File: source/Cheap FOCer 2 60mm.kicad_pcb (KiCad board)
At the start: 2 copper layers, 59.1 x 99.9 mm, 193 parts, among them J1 Conn_01x02, J2 Conn_01x07, J3 Conn_01x03, J4 On/Off, J5 UNUSED MCU PINS, J6 Conn_01x03, P1 MOTOR1, P2 MOTOR1, P3 MOTOR1, P4 HALL/Encoder, P5 SWD, Q1 NCEP60T20, Q2 NCEP60T20, Q3 NCEP60T20, Q4 NCEP60T20, Q5 NCEP60T20, Q6 NCEP60T20, U1 AMS1117-3.3, U2 DRV8301, U3 TP2604-SR, U4 TJA1051T/3/1J, U5 STM32F405RGT6, U6 BMI160, X1 8MHz 10ppm (X50328MSB2GI)

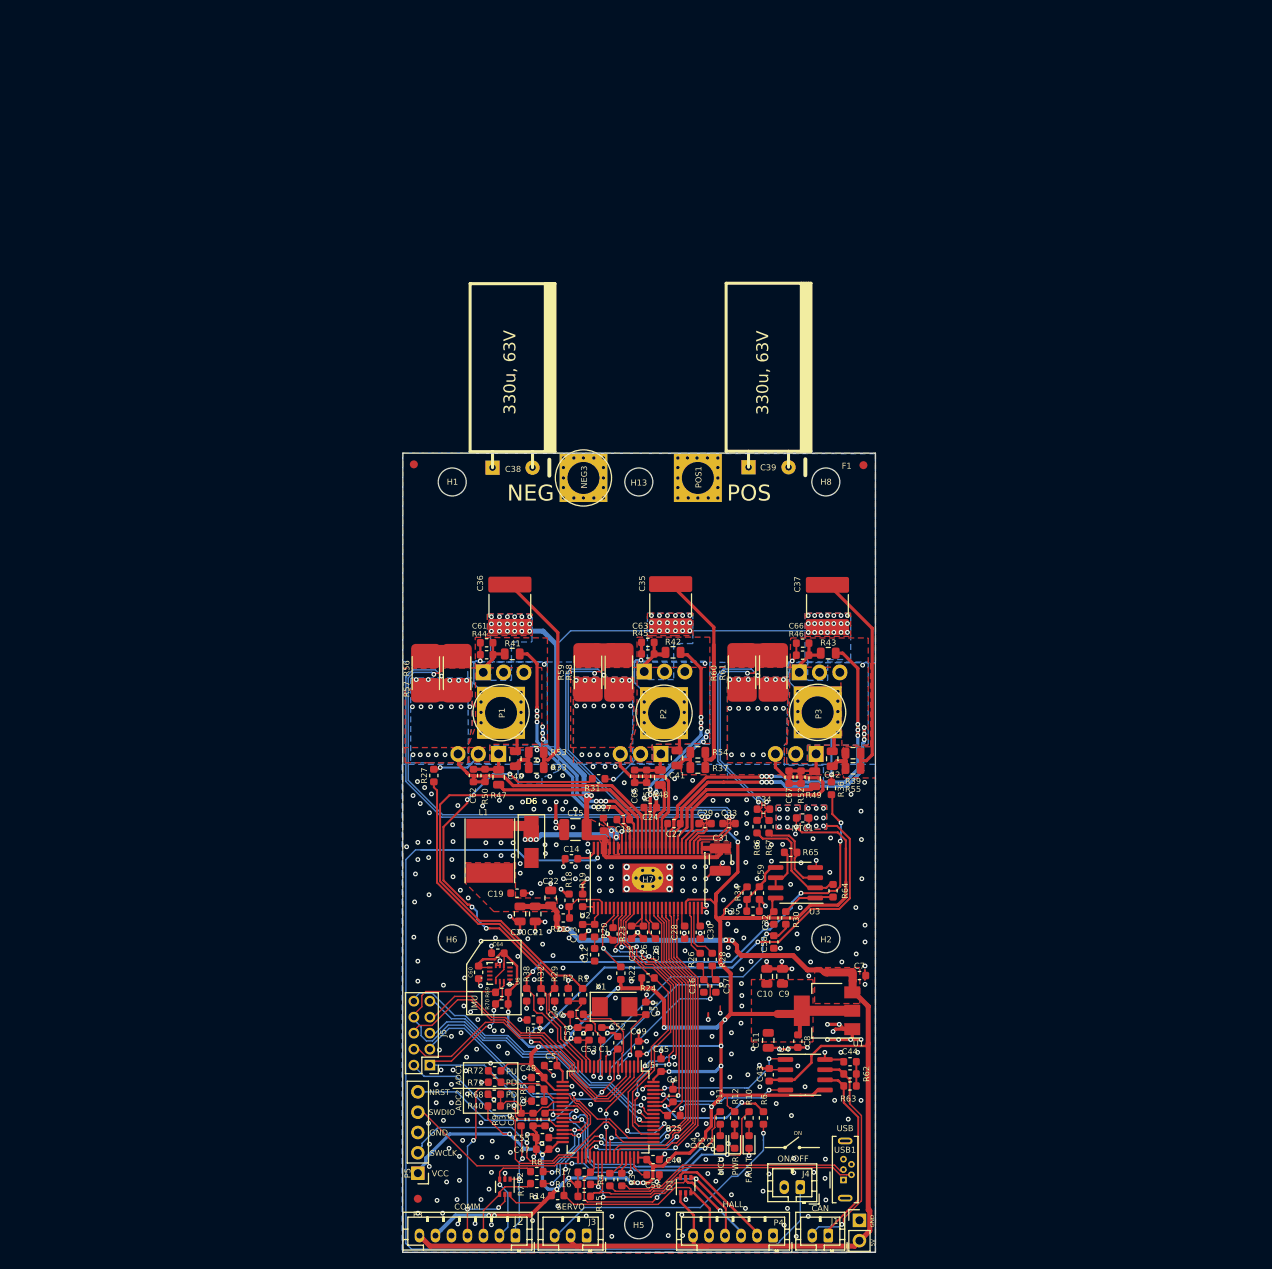
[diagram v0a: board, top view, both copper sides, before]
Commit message: started redrawing pcb
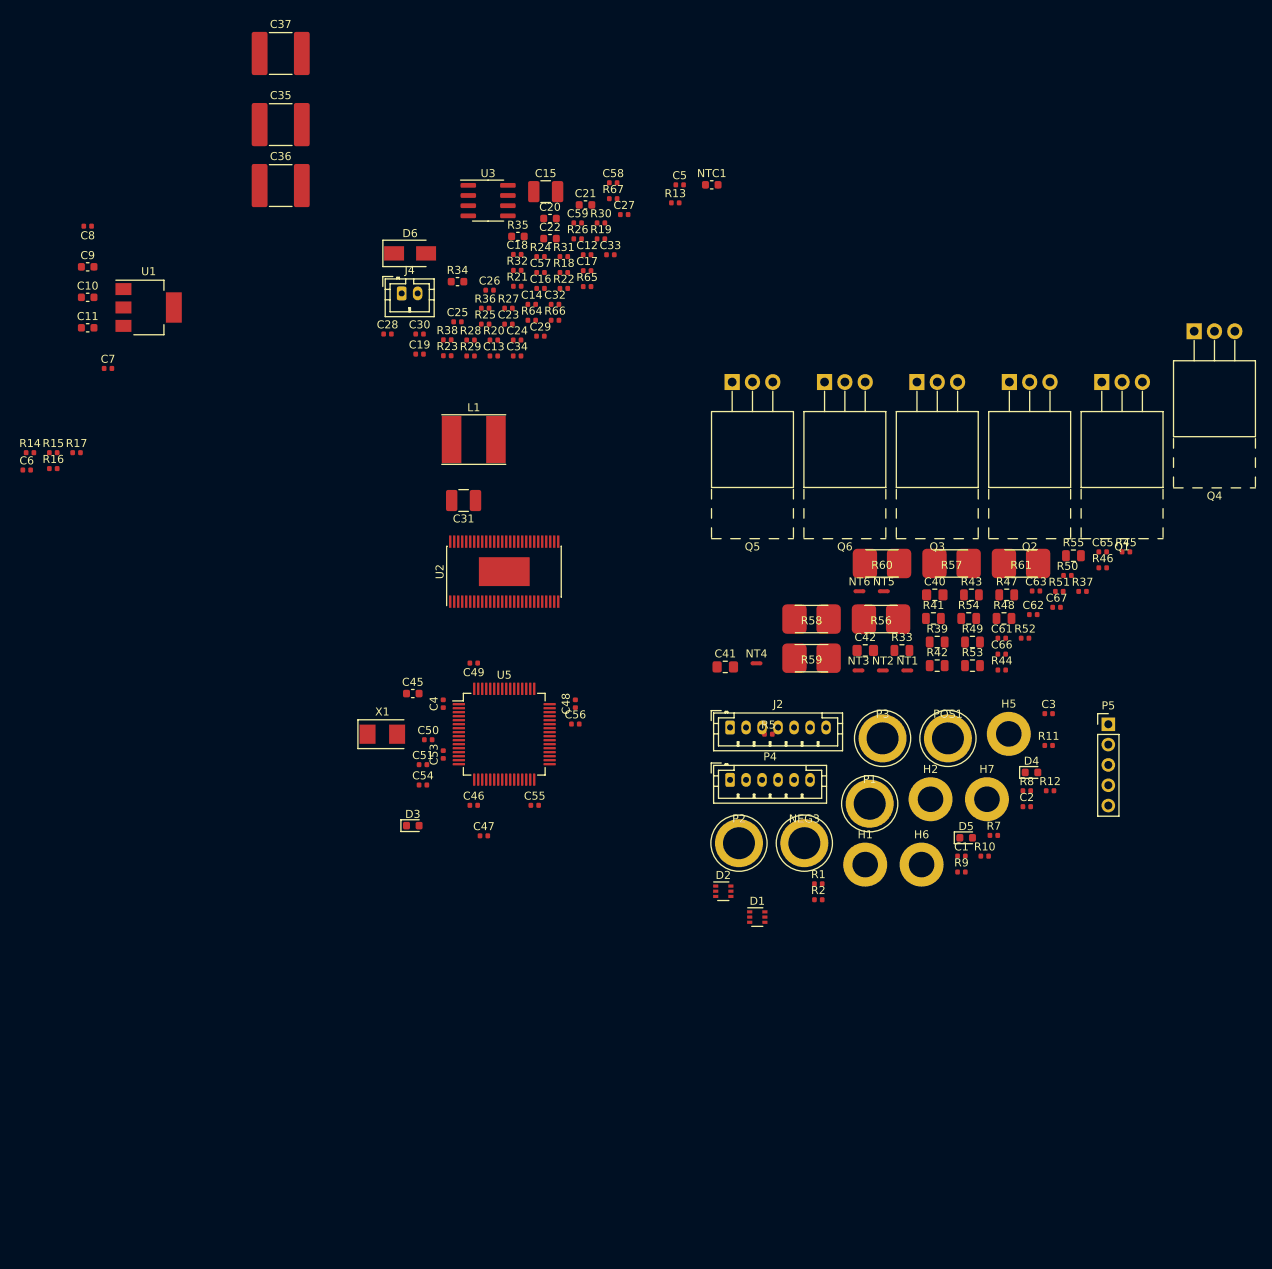
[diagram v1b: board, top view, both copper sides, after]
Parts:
- removed C38, C39: 330u, 63V, w_capacitors:CP_10x20mm_hor_with_model_brd_edge
- removed C43: 0.1u, Capacitor_SMD:C_0603_1608Metric
- removed C44: 1nF, Capacitor_SMD:C_0603_1608Metric
- removed C52, C60, C64: 100n, Capacitor_SMD:C_0603_1608Metric
- removed F1, F2, F3: Fiducial, Fiducial:Fiducial_1mm_Dia_2mm_Outer
- removed H13, H8: MountingHole, MountingHole:MountingHole_3.2mm_M3_ISO14580_Pad
- removed H3: SLJ, shapes3D:Sam_J
- removed H4: Open Hardware Logo, Symbol:OSHW-Logo2_9.8x8mm_SilkScreen
- removed H9: KiCAD Logo, Symbol:KiCad-Logo2_5mm_SilkScreen
- removed J1: Conn_01x02, Connector_JST:JST_PH_B2B-PH-K_1x02_P2.00mm_Vertical
- removed J3: Conn_01x03, Connector_JST:JST_PH_B3B-PH-K_1x03_P2.00mm_Vertical
- removed J5: UNUSED MCU PINS, Connector_PinHeader_2.00mm:PinHeader_2x05_P2.00mm_Vertical
- removed J6: Conn_01x03, Connector_PinHeader_2.54mm:PinHeader_1x02_P2.54mm_Vertical
- removed R3, R4: 22R, Resistor_SMD:R_0603_1608Metric
- removed R40, R68, R71, R72: DNP, Resistor_SMD:R_0603_1608Metric
- removed R6: 100R, Resistor_SMD:R_0603_1608Metric
- removed R62, R63: 60, Resistor_SMD:R_0603_1608Metric
- removed R69, R70: 1k, Resistor_SMD:R_0603_1608Metric
- removed U4: TJA1051T/3/1J, Package_SO:SOIC-8_3.9x4.9mm_P1.27mm
- removed U6: BMI160, Package_LGA:Bosch_LGA-14_3x2.5mm_P0.5mm
- removed USB1: USB Micro U-D-M5DD-W-1, Connector_USB:USB_Micro-B_Wuerth_614105150721_Vertical
- C1, C12, C14, C16, C17, C18, C19, C23, C24, C25, C26, C27, C28, C29, C30, C32, C33, C34, C5, C50, C51, C53, C54, C55, C56, C57, C58, C59, C6, C61, C62, C63, C65, C66, C67, C7, C8: footprint Capacitor_SMD:C_0603_1608Metric -> Capacitor_SMD:C_0402_1005Metric
- C10, C11, C20, C21, C22, C9: footprint Capacitor_SMD:C_0805_2012Metric -> Capacitor_SMD:C_0603_1608Metric
- C13: value 120p -> 150p; footprint Capacitor_SMD:C_0603_1608Metric -> Capacitor_SMD:C_0402_1005Metric
- C15, C31: footprint Capacitor_SMD:C_1210_3225Metric -> Capacitor_SMD:C_1210_3225Metric_Pad1.42x2.65mm_HandSolder
- C2, C3: value 0.01uF -> 10n; footprint Capacitor_SMD:C_0603_1608Metric -> Capacitor_SMD:C_0402_1005Metric
- C4: value .01uF -> 100n; footprint Capacitor_SMD:C_0603_1608Metric -> Capacitor_SMD:C_0402_1005Metric
- C40, C41, C42: footprint Capacitor_SMD:C_0805_2012Metric -> Capacitor_SMD:C_0805_2012Metric_Pad1.15x1.40mm_HandSolder
- C45: value 2.2u -> 10u
- C46, C47, C48, C49: value 2.2u -> 100n; footprint Capacitor_SMD:C_0603_1608Metric -> Capacitor_SMD:C_0402_1005Metric
- POS1, Q1, Q2, Q3, Q4, Q5, Q6: moved to F.Cu
- R1, R10, R11, R12, R13, R14, R15, R16, R17, R18, R19, R2, R20, R21, R22, R23, R24, R25, R26, R27, R28, R29, R30, R31, R32, R36, R38, R44, R45, R46, R5, R50, R51, R52, R64, R65, R66, R67, R7, R8, R9: footprint Resistor_SMD:R_0603_1608Metric -> Resistor_SMD:R_0402_1005Metric
- R37: footprint Resistor_SMD:R_0805_2012Metric -> Resistor_SMD:R_0402_1005Metric
- moved C8 135.1 mm to (71.2, 40.6), turned to 180 degrees
- moved C9 124.1 mm to (71.2, 45.7), turned to 0 degrees
- moved C11 123.2 mm to (71.2, 53.3), turned to 0 degrees
- moved J4 122.3 mm to (110.5, 49.0), turned to 0 degrees
- moved U1 122.1 mm to (78.8, 50.8), turned to 0 degrees
- moved C7 120.8 mm to (73.8, 58.4), turned to 0 degrees
- moved C10 120.0 mm to (71.2, 49.5), turned to 0 degrees
- moved R15 114.2 mm to (66.9, 68.9), turned to 0 degrees
- moved R14 113.9 mm to (64.0, 68.9), turned to 0 degrees
- moved R16 111.4 mm to (66.9, 70.9), turned to 0 degrees
- moved C5 111.3 mm to (145.2, 35.5), turned to 0 degrees
- moved R17 110.1 mm to (69.8, 68.9), turned to 0 degrees
- moved C6 103.9 mm to (63.6, 71.1), turned to 0 degrees
- moved R13 103.7 mm to (144.7, 37.7), turned to 0 degrees
- moved P5 102.9 mm to (198.8, 102.9), turned to 0 degrees
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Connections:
- C4 pad 2: /MCU/SERVO -> VCC
- U5 pad 2: PC13 -> Net-(U5-Pad2)
- U5 pad 25: PC5 -> Net-(U5-Pad25)
- U5 pad 28: PB2 -> /MCU/PB2
- U5 pad 3: PC14 -> Net-(U5-Pad3)
- U5 pad 33: PB12 -> Net-(U5-Pad33)
- U5 pad 4: PC15 -> Net-(U5-Pad4)
- U5 pad 50: PA15 -> /MCU/PA15
- U5 pad 54: PD2 -> Net-(U5-Pad54)
- U5 pad 55: PB3 -> Net-(U5-Pad55)
- U5 pad 56: PB4 -> Net-(U5-Pad56)
- U5 pad 61: /CAN bus transceiver/CAN_RX -> /MCU/CAN_RX
- U5 pad 62: /CAN bus transceiver/CAN_TX -> /MCU/CAN_TX
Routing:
- net VCC: track 358.3 -> 0.00 mm, vias 31 -> 0
- net GND: track 236.2 -> 0.00 mm, vias 383 -> 0
- net +5V: track 181.2 -> 0.00 mm, vias 4 -> 0
- net V_SUPPLY: track 143.5 -> 0.00 mm, vias 75 -> 0
- net Net-(J4-Pad1): track 129.7 -> 0.00 mm, vias 1 -> 0
- net /Mosfet driver/H3_VS: track 80.5 -> 0.00 mm, vias 19 -> 0
- net /MCU/SENS3: track 70.4 -> 0.00 mm, vias 4 -> 0
- net /MCU/ADC_TEMP: track 70.0 -> 0.00 mm, vias 11 -> 0
- net SPA: track 63.3 -> 0.00 mm, vias 2 -> 0
- net SNA: track 63.0 -> 0.00 mm, vias 2 -> 0
- net /MCU/SENS2: track 60.9 -> 0.00 mm, vias 4 -> 0
- net PA15: track 53.7 -> 0.00 mm, vias 1 -> 0
- net /Mosfet driver/H1_VS: track 52.7 -> 0.00 mm, vias 19 -> 0
- net /Mosfet driver/GH_C: track 52.3 -> 0.00 mm, vias 6 -> 0
- net /Mosfet driver/H1_LOW: track 49.9 -> 0.00 mm, vias 17 -> 0
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- removed copper zone on F.Cu, net +5V
- removed copper zone on B.Cu, net /MCU/ADC_TEMP
- removed copper zone on F.Cu, net /MCU/ADC_TEMP
- removed copper zone on B.Cu, net /Mosfet driver/H1_LOW
- removed copper zone on F.Cu, net /Mosfet driver/H1_LOW
- removed copper zone on B.Cu, net /Mosfet driver/H1_VS
- removed copper zone on F.Cu, net /Mosfet driver/H1_VS
- removed copper zone on B.Cu, net /Mosfet driver/H2_LOW
- removed copper zone on F.Cu, net /Mosfet driver/H2_LOW
- removed copper zone on B.Cu, net /Mosfet driver/H2_VS
- removed copper zone on F.Cu, net /Mosfet driver/H2_VS
- removed copper zone on B.Cu, net /Mosfet driver/H3_LOW
- removed copper zone on F.Cu, net /Mosfet driver/H3_LOW
- removed copper zone on B.Cu, net /Mosfet driver/H3_VS
- removed copper zone on F.Cu, net /Mosfet driver/H3_VS
- removed copper zone on B.Cu, net GND
- removed copper zone on F.Cu, net GND
- removed copper zone on F.Cu, net Net-(C17-Pad2)
- removed copper zone on B.Cu, net VCC
- removed copper zone on F.Cu, net VCC
- removed copper zone on B.Cu, net V_SUPPLY
- removed copper zone on F.Cu, net V_SUPPLY
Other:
- board outline removed
- board text removed: "5V"
- board text removed: "ADC1"
- board text removed: "ADC2"
- board text removed: "CAN"
- board text removed: "CHEAP FOCER 2"
- board text removed: "COMM"
- board text removed: "FAULT"
- board text removed: "GND"
- board text removed: "HALL"
- board text removed: "IMU"
- board text removed: "MCU"
- board text removed: "NEG"
- board text removed: "NRST"
- board text removed: "ON"
- board text removed: "ON/OFF"
- board text removed: "PD"
- board text removed: "POS"
- board text removed: "PU"
- board text removed: "PWR"
- board text removed: "SERVO"
- board text removed: "SWCLK"
- board text removed: "SWDIO"
- board text removed: "USB"
- board text removed: "VCC"
